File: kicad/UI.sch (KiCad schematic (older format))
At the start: 13 parts, among them Q4 BSS138, SW3 BUTTON

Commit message: 新基板，部品を配置
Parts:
- added D14, D15: LED, LEDs:LED_0603, symbol LED
- added R22, R23: 1k, Resistors_SMD:R_0402, symbol R
- renumbered R22 to R24
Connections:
- net GND: now also D14.1 (K), D15.1 (K)
- new net: D14.2 (A), R22.2
- new net: D15.2 (A), R23.2
- new net LED_5: R22.1
- new net LED_6: R23.1
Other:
- moved on the sheet: C32, D10, D11, D12, D13, R18, R19, R20, R21, SW3

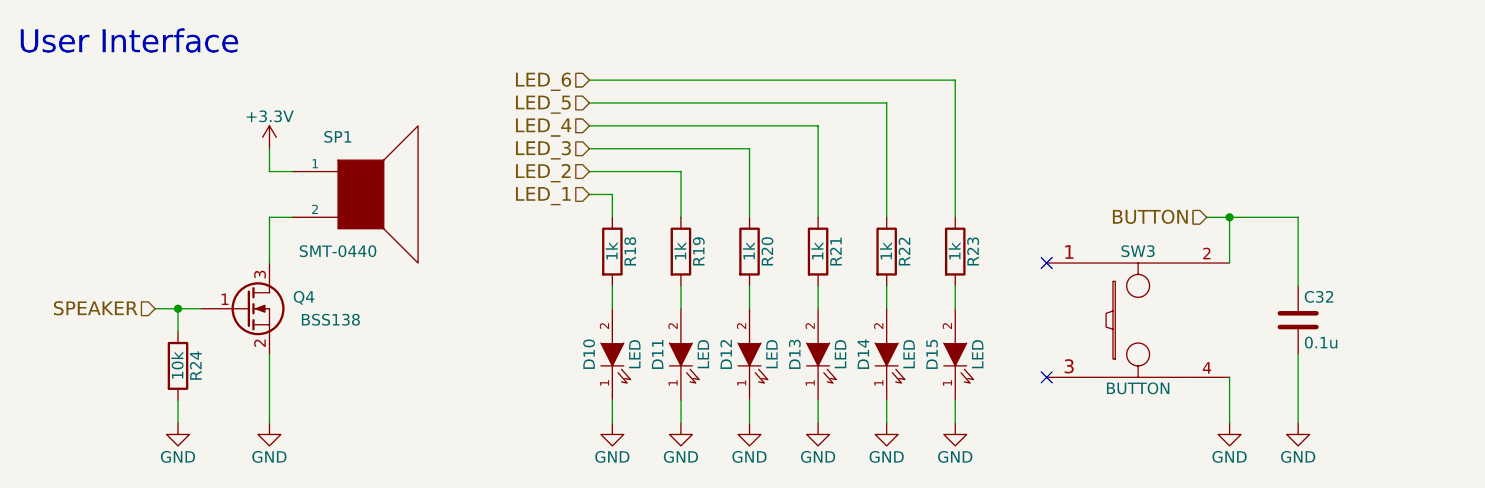
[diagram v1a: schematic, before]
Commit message: 自動配線用にdsn吐き出し
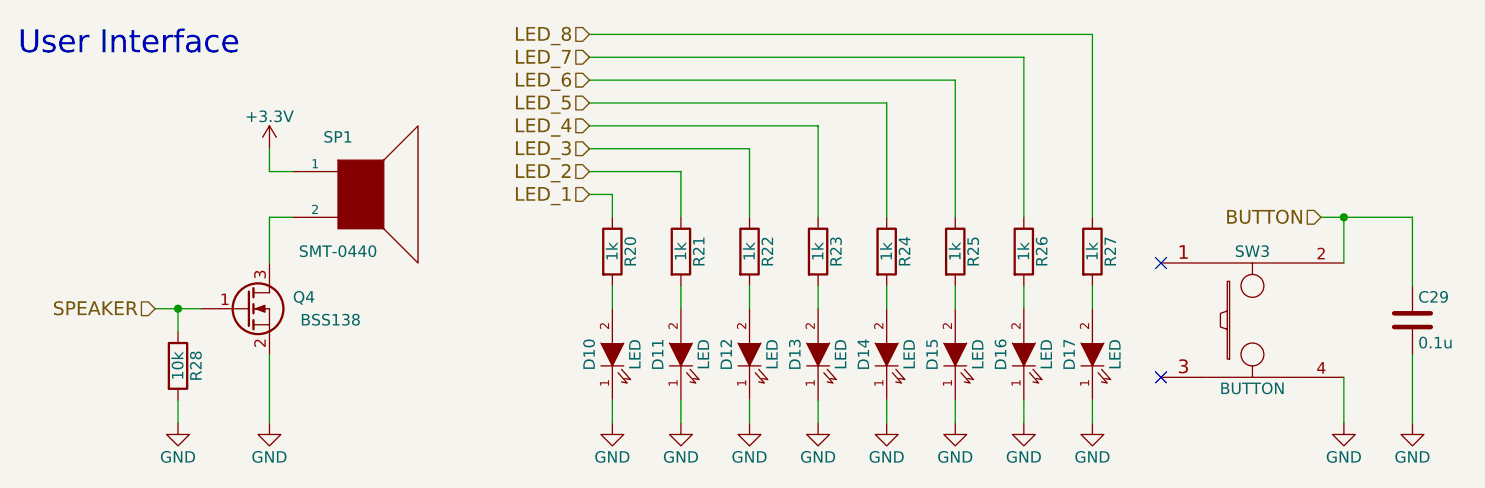
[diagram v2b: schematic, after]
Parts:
- added D16, D17: LED, LEDs:LED_0603, symbol LED
- added R26, R27: 1k, Resistors_SMD:R_0402, symbol R
- renumbered C32 to C29, R18 to R20, R19 to R21, R20 to R22, R21 to R23, R22 to R24, R23 to R25, R24 to R28
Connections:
- net GND: now also D16.1 (K), D17.1 (K)
- new net: D16.2 (A), R26.2
- new net: D17.2 (A), R27.2
- new net LED_7: R26.1
- new net LED_8: R27.1
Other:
- moved on the sheet: C29, SW3
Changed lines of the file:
@@
 $EndComp
 $Comp
-L +3.3V #PWR092
+L +3.3V #PWR088
 U 1 1 57CE7538
 P 4400 3500
-F 0 "#PWR092" H 4400 3350 50  0001 C CNN
+F 0 "#PWR088" H 4400 3350 50  0001 C CNN
 F 1 "+3.3V" H 4400 3640 50  0000 C CNN
 F 2 "" H 4400 3500 50  0000 C CNN
@@
 $EndComp
 $Comp
-L R R24
+L R R28
 U 1 1 57CE757A
 P 4000 4450
-F 0 "R24" V 4080 4450 50  0000 C CNN
+F 0 "R28" V 4080 4450 50  0000 C CNN
 F 1 "10k" V 4000 4450 50  0000 C CNN
 F 2 "Resistors_SMD:R_0402" V 3930 4450 50  0001 C CNN
@@
 $EndComp
 $Comp
-L GND #PWR093
+L GND #PWR089
 U 1 1 57CE7673
 P 4400 4700
-F 0 "#PWR093" H 4400 4450 50  0001 C CNN
+F 0 "#PWR089" H 4400 4450 50  0001 C CNN
 F 1 "GND" H 4400 4550 50  0000 C CNN
 F 2 "" H 4400 4700 50  0000 C CNN
@@
 $EndComp
 $Comp
-L GND #PWR094
+L GND #PWR090
 U 1 1 57CE768B
 P 4000 4700
-F 0 "#PWR094" H 4000 4450 50  0001 C CNN
+F 0 "#PWR090" H 4000 4450 50  0001 C CNN
 F 1 "GND" H 4000 4550 50  0000 C CNN
 F 2 "" H 4000 4700 50  0000 C CNN
@@
 $EndComp
 $Comp
-L GND #PWR095
+L GND #PWR091
 U 1 1 57CE8530
 P 5900 4700
-F 0 "#PWR095" H 5900 4450 50  0001 C CNN
+F 0 "#PWR091" H 5900 4450 50  0001 C CNN
 F 1 "GND" H 5900 4550 50  0000 C CNN
 F 2 "" H 5900 4700 50  0000 C CNN
@@
 $EndComp
 $Comp
-L GND #PWR096
+L GND #PWR092
 U 1 1 57CE8557
 P 6200 4700
-F 0 "#PWR096" H 6200 4450 50  0001 C CNN
+F 0 "#PWR092" H 6200 4450 50  0001 C CNN
 F 1 "GND" H 6200 4550 50  0000 C CNN
 F 2 "" H 6200 4700 50  0000 C CNN
@@
 $EndComp
 $Comp
-L GND #PWR097
+L GND #PWR093
 U 1 1 57CE8577
 P 6500 4700
-F 0 "#PWR097" H 6500 4450 50  0001 C CNN
+F 0 "#PWR093" H 6500 4450 50  0001 C CNN
 F 1 "GND" H 6500 4550 50  0000 C CNN
 F 2 "" H 6500 4700 50  0000 C CNN
@@
 $EndComp
 $Comp
-L GND #PWR098
+L GND #PWR094
 U 1 1 57CE8597
 P 6800 4700
-F 0 "#PWR098" H 6800 4450 50  0001 C CNN
+F 0 "#PWR094" H 6800 4450 50  0001 C CNN
 F 1 "GND" H 6800 4550 50  0000 C CNN
 F 2 "" H 6800 4700 50  0000 C CNN
@@
 	5900 4600 5900 4700
 $Comp
-L R R18
+L R R20
 U 1 1 57CE8600
 P 5900 3950
-F 0 "R18" V 5980 3950 50  0000 C CNN
+F 0 "R20" V 5980 3950 50  0000 C CNN
 F 1 "1k" V 5900 3950 50  0000 C CNN
 F 2 "Resistors_SMD:R_0402" V 5830 3950 50  0001 C CNN
@@
 $EndComp
 $Comp
-L R R19
+L R R21
 U 1 1 57CE8644
 P 6200 3950
-F 0 "R19" V 6280 3950 50  0000 C CNN
+F 0 "R21" V 6280 3950 50  0000 C CNN
 F 1 "1k" V 6200 3950 50  0000 C CNN
 F 2 "Resistors_SMD:R_0402" V 6130 3950 50  0001 C CNN
@@
 $EndComp
 $Comp
-L R R20
+L R R22
 U 1 1 57CE8677
 P 6500 3950
-F 0 "R20" V 6580 3950 50  0000 C CNN
+F 0 "R22" V 6580 3950 50  0000 C CNN
 F 1 "1k" V 6500 3950 50  0000 C CNN
 F 2 "Resistors_SMD:R_0402" V 6430 3950 50  0001 C CNN
@@
 $EndComp
 $Comp
-L R R21
+L R R23
 U 1 1 57CE86AD
 P 6800 3950
-F 0 "R21" V 6880 3950 50  0000 C CNN
+F 0 "R23" V 6880 3950 50  0000 C CNN
 F 1 "1k" V 6800 3950 50  0000 C CNN
 F 2 "Resistors_SMD:R_0402" V 6730 3950 50  0001 C CNN
@@
 	6800 3400 6800 3800
 $Comp
-L GND #PWR099
+L GND #PWR095
 U 1 1 57CEA2EF
-P 8600 4700
-F 0 "#PWR099" H 8600 4450 50  0001 C CNN
-F 1 "GND" H 8600 4550 50  0000 C CNN
-F 2 "" H 8600 4700 50  0000 C CNN
-F 3 "" H 8600 4700 50  0000 C CNN
-	1    8600 4700
-	1    0    0    -1
-$EndComp
-Wire Wire Line
-	8600 4700 8600 4500
-Text HLabel 8500 3800 0    60   Input ~ 0
+P 9100 4700
+F 0 "#PWR095" H 9100 4450 50  0001 C CNN
+F 1 "GND" H 9100 4550 50  0000 C CNN
+F 2 "" H 9100 4700 50  0000 C CNN
+F 3 "" H 9100 4700 50  0000 C CNN
+	1    9100 4700
+	1    0    0    -1
+$EndComp
+Wire Wire Line
+	9100 4700 9100 4500
+Text HLabel 9000 3800 0    60   Input ~ 0
 BUTTON
 $Comp
 L Tactile_SW_4P SW3
 U 1 1 57DDE1FB
-P 8200 4200
-F 0 "SW3" H 8200 4450 50  0000 C CNN
-F 1 "BUTTON" H 8200 3850 50  0000 C CNN
-F 2 "mouse:SW_PUSH" V 8150 4150 60  0001 C CNN
-F 3 "" V 8150 4150 60  0000 C CNN
-	1    8200 4200
-	1    0    0    -1
-$EndComp
-NoConn ~ 7800 4000
-NoConn ~ 7800 4500
+P 8700 4200
+F 0 "SW3" H 8700 4450 50  0000 C CNN
+F 1 "BUTTON" H 8700 3850 50  0000 C CNN
+F 2 "mouse:SW_PUSH" V 8650 4150 60  0001 C CNN
+F 3 "" V 8650 4150 60  0000 C CNN
+	1    8700 4200
+	1    0    0    -1
+$EndComp
+NoConn ~ 8300 4000
+NoConn ~ 8300 4500
 Text Notes 3300 3100 0    100  ~ 0
 User Interface
 Wire Wire Line
-	8600 3800 8600 4000
-Wire Wire Line
-	8500 3800 8900 3800
-$Comp
-L GND #PWR0100
+	9100 3800 9100 4000
+Wire Wire Line
+	9000 3800 9400 3800
+$Comp
+L GND #PWR096
 U 1 1 57CEAAF6
-P 8900 4700
-F 0 "#PWR0100" H 8900 4450 50  0001 C CNN
-F 1 "GND" H 8900 4550 50  0000 C CNN
-F 2 "" H 8900 4700 50  0000 C CNN
-F 3 "" H 8900 4700 50  0000 C CNN
-	1    8900 4700
-	1    0    0    -1
-$EndComp
-$Comp
-L C C32
+P 9400 4700
+F 0 "#PWR096" H 9400 4450 50  0001 C CNN
+F 1 "GND" H 9400 4550 50  0000 C CNN
+F 2 "" H 9400 4700 50  0000 C CNN
+F 3 "" H 9400 4700 50  0000 C CNN
+	1    9400 4700
+	1    0    0    -1
+$EndComp
+$Comp
+L C C29
 U 1 1 583A7129
-P 8900 4250
-F 0 "C32" H 8925 4350 50  0000 L CNN
-F 1 "0.1u" H 8925 4150 50  0000 L CNN
-F 2 "Capacitors_SMD:C_0402" H 8938 4100 50  0001 C CNN
-F 3 "" H 8900 4250 50  0000 C CNN
-	1    8900 4250
-	1    0    0    -1
-$EndComp
-Wire Wire Line
-	8900 4400 8900 4700
-Wire Wire Line
-	8900 3800 8900 4100
-Connection ~ 8600 3800
+P 9400 4250
+F 0 "C29" H 9425 4350 50  0000 L CNN
+F 1 "0.1u" H 9425 4150 50  0000 L CNN
+F 2 "Capacitors_SMD:C_0402" H 9438 4100 50  0001 C CNN
+F 3 "" H 9400 4250 50  0000 C CNN
+	1    9400 4250
+	1    0    0    -1
+$EndComp
+Wire Wire Line
+	9400 4400 9400 4700
+Wire Wire Line
+	9400 3800 9400 4100
+Connection ~ 9100 3800
 $Comp
 L LED D14
@@
 $EndComp
 $Comp
-L GND #PWR0101
+L GND #PWR097
 U 1 1 5860C878
 P 7100 4700
-F 0 "#PWR0101" H 7100 4450 50  0001 C CNN
+F 0 "#PWR097" H 7100 4450 50  0001 C CNN
 F 1 "GND" H 7100 4550 50  0000 C CNN
 F 2 "" H 7100 4700 50  0000 C CNN
@@
 $EndComp
 $Comp
-L GND #PWR0102
+L GND #PWR098
 U 1 1 5860C8B0
 P 7400 4700
-F 0 "#PWR0102" H 7400 4450 50  0001 C CNN
+F 0 "#PWR098" H 7400 4450 50  0001 C CNN
 F 1 "GND" H 7400 4550 50  0000 C CNN
 F 2 "" H 7400 4700 50  0000 C CNN
@@
 	7100 4600 7100 4700
 $Comp
-L R R22
+L R R24
 U 1 1 5860C949
 P 7100 3950
-F 0 "R22" V 7180 3950 50  0000 C CNN
+F 0 "R24" V 7180 3950 50  0000 C CNN
 F 1 "1k" V 7100 3950 50  0000 C CNN
 F 2 "Resistors_SMD:R_0402" V 7030 3950 50  0001 C CNN
@@
 $EndComp
 $Comp
-L R R23
+L R R25
 U 1 1 5860C991
 P 7400 3950
-F 0 "R23" V 7480 3950 50  0000 C CNN
+F 0 "R25" V 7480 3950 50  0000 C CNN
 F 1 "1k" V 7400 3950 50  0000 C CNN
 F 2 "Resistors_SMD:R_0402" V 7330 3950 50  0001 C CNN
@@
 Wire Wire Line
 	7400 3200 5800 3200
+$Comp
+L LED D16
+U 1 1 5867454B
+P 7700 4400
+F 0 "D16" H 7700 4500 50  0000 C CNN
+F 1 "LED" H 7700 4300 50  0000 C CNN
+F 2 "LEDs:LED_0603" H 7700 4400 50  0001 C CNN
+F 3 "" H 7700 4400 50  0000 C CNN
+	1    7700 4400
+	0    -1   -1   0
+$EndComp
+$Comp
+L LED D17
+U 1 1 58674599
+P 8000 4400
+F 0 "D17" H 8000 4500 50  0000 C CNN
+F 1 "LED" H 8000 4300 50  0000 C CNN
+F 2 "LEDs:LED_0603" H 8000 4400 50  0001 C CNN
+F 3 "" H 8000 4400 50  0000 C CNN
+	1    8000 4400
+	0    -1   -1   0
+$EndComp
+$Comp
+L GND #PWR099
+U 1 1 58674609
+P 7700 4700
+F 0 "#PWR099" H 7700 4450 50  0001 C CNN
+F 1 "GND" H 7700 4550 50  0000 C CNN
+F 2 "" H 7700 4700 50  0000 C CNN
+F 3 "" H 7700 4700 50  0000 C CNN
+	1    7700 4700
+	1    0    0    -1
+$EndComp
+$Comp
+L GND #PWR0100
+U 1 1 5867464D
+P 8000 4700
+F 0 "#PWR0100" H 8000 4450 50  0001 C CNN
+F 1 "GND" H 8000 4550 50  0000 C CNN
+F 2 "" H 8000 4700 50  0000 C CNN
+F 3 "" H 8000 4700 50  0000 C CNN
+	1    8000 4700
+	1    0    0    -1
+$EndComp
+Wire Wire Line
+	8000 4700 8000 4600
+Wire Wire Line
+	7700 4600 7700 4700
+$Comp
+L R R26
+U 1 1 5867470A
+P 7700 3950
+F 0 "R26" V 7780 3950 50  0000 C CNN
+F 1 "1k" V 7700 3950 50  0000 C CNN
+F 2 "Resistors_SMD:R_0402" V 7630 3950 50  0001 C CNN
+F 3 "" H 7700 3950 50  0000 C CNN
+	1    7700 3950
+	1    0    0    -1
+$EndComp
+$Comp
+L R R27
+U 1 1 5867475E
+P 8000 3950
+F 0 "R27" V 8080 3950 50  0000 C CNN
+F 1 "1k" V 8000 3950 50  0000 C CNN
+F 2 "Resistors_SMD:R_0402" V 7930 3950 50  0001 C CNN
+F 3 "" H 8000 3950 50  0000 C CNN
+	1    8000 3950
+	1    0    0    -1
+$EndComp
+Wire Wire Line
+	8000 4100 8000 4200
+Wire Wire Line
+	7700 4200 7700 4100
+Text HLabel 5800 3100 0    60   Input ~ 0
+LED_7
+Text HLabel 5800 3000 0    60   Input ~ 0
+LED_8
+Wire Wire Line
+	5800 3100 7700 3100
+Wire Wire Line
+	7700 3100 7700 3800
+Wire Wire Line
+	8000 3800 8000 3000
+Wire Wire Line
+	8000 3000 5800 3000
 $EndSCHEMATC
